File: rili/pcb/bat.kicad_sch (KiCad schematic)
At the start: 21 parts, among them J1 Battery, Q3 AO3407, Q4 FS8205, SW1 SW_SPDT, U3 TP4056-42-ESOP8, U4 MCP1700x-330xxTT, U5 DW01A

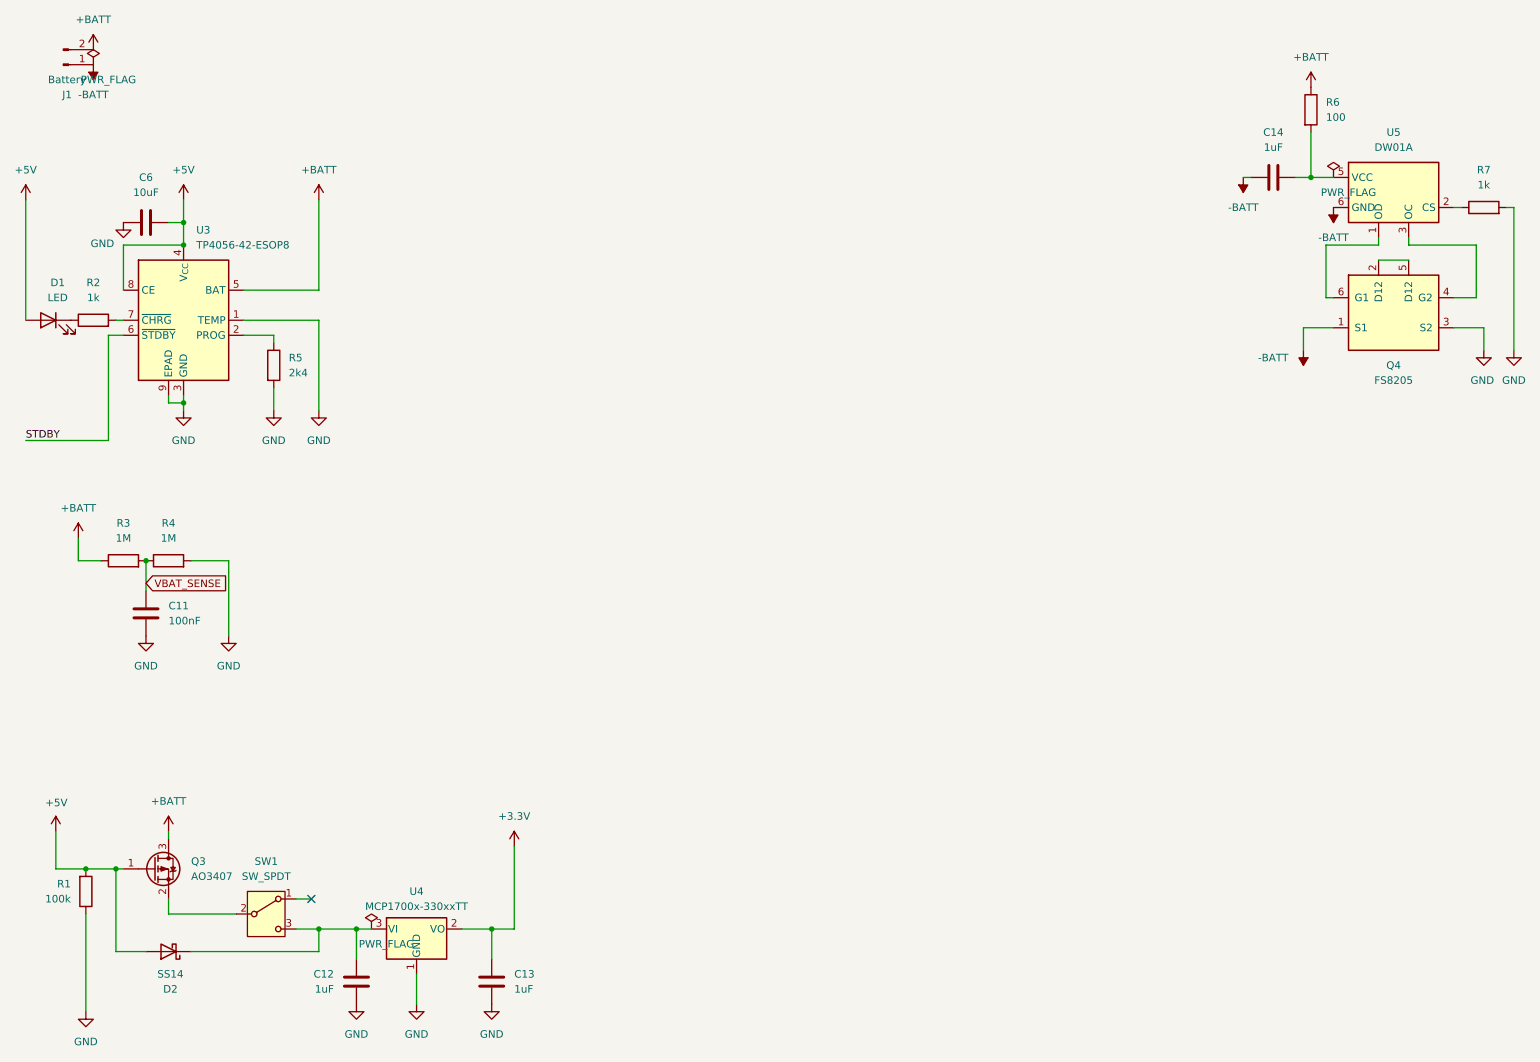
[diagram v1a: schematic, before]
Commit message: layout v2 : carte routée — PCB↔schéma réconciliés, BOM LCSC, TVS matrice, DRC 990→24
- réconciliation PCB↔schéma en une passe : 105 empreintes remariées (matrice ×2,
  module P4), 54 périmées supprimées, ~140 importées par F8 ; footprint TRRS
  MJ-4PP-9_rev3 créé (pads mappés de l'ancien design fonctionnel)
- placement : moitié droite générée au miroir exact du pré-placement gauche
  (axe x=188.46048), trous de montage symétrisés, origine de grille sur l'axe
- protection ESD matrice : 22 SD05C-01F (un par ligne, côté switchs des 100R,
  validés par partition de netlist) ; PWR_FLAG +5V_D réparé
- BOM LCSC dans les propriétés des symboles (32 composants : réfs, liens,
  notes d'achat) + annexe courses complète au plan v2 ; connecteur trackpad
  corrigé (ZIF Hirose FH12-6S-0.5SH, réf MNT Reform)
- règles JLCPCB (planchers DRC + classes Default/Power re-branchées v2),
  passage 4 couches, routage complet des deux moitiés
- gerbers v1 corne-cherry retirés (obsolètes)
- baselines tripwire re-référencées : DRC 990→24 erreurs / 208→17 warnings,
  ERC 0 erreur / 200 warnings (53 fantômes headless documentés)

Co-Authored-By: Claude Fable 5 <noreply@anthropic.com>
Claude-Session: https://claude.ai/code/session_01GfX5RmekmQi78Dm37qsT4Z
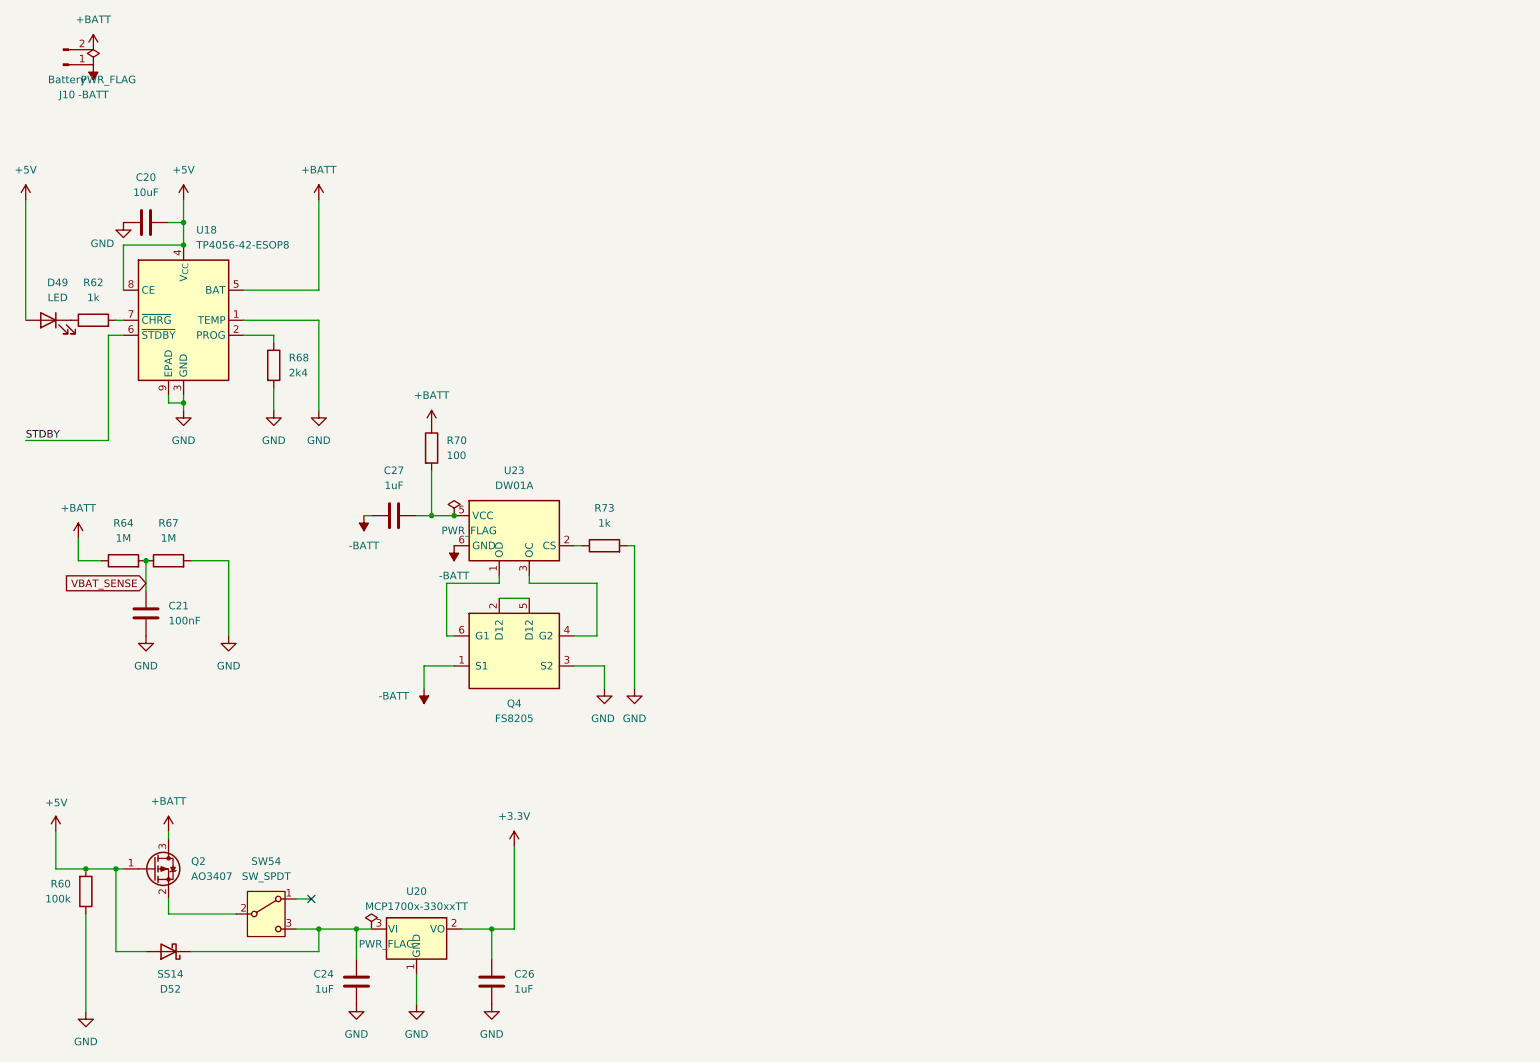
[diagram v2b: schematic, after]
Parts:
- C20: renamed from C6; footprint Capacitor_SMD:C_1210_3225Metric_Pad1.33x2.70mm_HandSolder -> Capacitor_SMD:C_1206_3216Metric_Pad1.33x1.80mm_HandSolder
- D52: renamed from D2; LCSC (none) -> C2480; Lien (none) -> https://lcsc.com/product-detail/C2480.html
- Q2: renamed from Q3; LCSC (none) -> C351408; Lien (none) -> https://lcsc.com/product-detail/C351408.html
- Q4: LCSC (none) -> C32254; Lien (none) -> https://lcsc.com/product-detail/C32254.html
- SW54: renamed from SW1; LCSC (none) -> C431540; Lien (none) -> https://lcsc.com/product-detail/C431540.html; Note achat (none) -> MSK-12C02 SHOU HAN
- U18: renamed from U3; LCSC (none) -> C16581; Lien (none) -> https://lcsc.com/product-detail/C16581.html
- U20: renamed from U4; LCSC (none) -> C39051; Lien (none) -> https://lcsc.com/product-detail/C39051.html
- U23: renamed from U5; LCSC (none) -> C351410; Lien (none) -> https://lcsc.com/product-detail/C351410.html
- renumbered C11 to C21, C12 to C24, C13 to C26, C14 to C27, D1 to D49, J1 to J10, R1 to R60, R2 to R62, R3 to R64, R4 to R67, R5 to R68, R6 to R70, R7 to R73
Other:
- moved on the sheet: C27, Q4, R70, R73, U23

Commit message: layout : panneau vertical 2 rails dans le dépôt + baseline chantier
Panneau 185×212 (droite tournée 180°, rails + 8 tabs mouse-bites) appliqué par
Mae, F8 des passifs unifiés. Baseline DRC re-référencée 24/19 → 36/26 (état
panneau, finitions DRC prévues : pistes près des lignes de rupture, vias de
maillage orphelins dans les bandes sans cuivre).

Co-Authored-By: Claude Fable 5 <noreply@anthropic.com>
Claude-Session: https://claude.ai/code/session_01GfX5RmekmQi78Dm37qsT4Z
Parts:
- C21: footprint Capacitor_SMD:C_0805_2012Metric_Pad1.18x1.45mm_HandSolder -> Capacitor_SMD:C_0603_1608Metric
- R60, R70: footprint Resistor_SMD:R_0805_2012Metric_Pad1.20x1.40mm_HandSolder -> Resistor_SMD:R_0603_1608Metric
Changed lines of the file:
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@@
 			)
 		)
-		(property "Footprint" "Resistor_SMD:R_0805_2012Metric_Pad1.20x1.40mm_HandSolder"
+		(property "Footprint" "Resistor_SMD:R_0603_1608Metric"
 			(at 28.702 163.83 90)
 			(hide yes)
@@
 			)
 		)
-		(property "Footprint" "Resistor_SMD:R_0805_2012Metric_Pad1.20x1.40mm_HandSolder"
+		(property "Footprint" "Resistor_SMD:R_0603_1608Metric"
 			(at 87.122 88.9 90)
 			(hide yes)
@@
 			)
 		)
-		(property "Footprint" "Capacitor_SMD:C_0805_2012Metric_Pad1.18x1.45mm_HandSolder"
+		(property "Footprint" "Capacitor_SMD:C_0603_1608Metric"
 			(at 39.6748 113.03 0)
 			(hide yes)

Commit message: review schéma : LDO S3 corrigé (pins SOT-89) + 8 valeurs — HT7833 en place
Revue 4 relecteurs parallèles avant commande, validée ligne à ligne sur la
netlist. BLOQUANT réparé : U20/U21 avaient le brochage SOT-23 du MCP1700 sur
des pastilles SOT-89 → entrée/sortie inversées pour tout LDO réel ; pins 2/3
échangés dans la déf, Value=HT7833 (C50936), F8 + reroutage des 2 zones par
Mae, pads vérifiés (1=GND 2=VIN 3=VOUT). Valeurs : bulk 3V3 C11/C12 et condos
LDO C23-C26 → 10µF (C15850), CHIP_PU P4 R54→10k C14→1µF. Baseline ERC 200→202
(lib_symbol_mismatch des défs LDO éditées). Validé par la revue : chaînes
batterie/charge/load-share, paires USB bout en bout, hub, prog P4 ×2 ports,
microSD IOMUX+pullups, strapping, nRF24, trackpad, 22 TVS matrice.

Co-Authored-By: Claude Fable 5 <noreply@anthropic.com>
Claude-Session: https://claude.ai/code/session_01GfX5RmekmQi78Dm37qsT4Z
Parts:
- C21: footprint Capacitor_SMD:C_0603_1608Metric -> Capacitor_SMD:C_0603_1608Metric_Pad1.08x0.95mm_HandSolder
- C24, C26: value 1uF -> 10uF; footprint Capacitor_SMD:C_0805_2012Metric_Pad1.18x1.45mm_HandSolder -> Capacitor_SMD:C_1206_3216Metric_Pad1.33x1.80mm_HandSolder
- R60, R70: footprint Resistor_SMD:R_0603_1608Metric -> Resistor_SMD:R_0603_1608Metric_Pad0.98x0.95mm_HandSolder
- U20: value MCP1700x-330xxTT -> HT7833; LCSC C39051 -> C50936; Lien https://lcsc.com/product-detail/C39051.html -> https://lcsc.com/product-detail/C50936.html
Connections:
- net +3.3V: now also U20.3 (VO); no longer U20.2 (VO)
- net at C24.2, D52.1 (K), SW54.3 (C): now also U20.2 (VI); no longer U20.3 (VI)
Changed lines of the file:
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@@
 			)
 		)
-		(property "Footprint" "Resistor_SMD:R_0603_1608Metric"
+		(property "Footprint" "Resistor_SMD:R_0603_1608Metric_Pad0.98x0.95mm_HandSolder"
 			(at 28.702 163.83 90)
 			(hide yes)
@@
 			)
 		)
-		(property "Footprint" "Resistor_SMD:R_0603_1608Metric"
+		(property "Footprint" "Resistor_SMD:R_0603_1608Metric_Pad0.98x0.95mm_HandSolder"
 			(at 87.122 88.9 90)
 			(hide yes)
@@
 			)
 		)
-		(property "Value" "1uF"
+		(property "Value" "10uF"
 			(at 102.87 180.3399 0)
 			(show_name no)
@@
 			)
 		)
-		(property "Footprint" "Capacitor_SMD:C_0805_2012Metric_Pad1.18x1.45mm_HandSolder"
+		(property "Footprint" "Capacitor_SMD:C_1206_3216Metric_Pad1.33x1.80mm_HandSolder"
 			(at 98.0948 175.26 0)
 			(hide yes)
@@
 			)
 		)
-		(property "Value" "1uF"
+		(property "Value" "10uF"
 			(at 72.39 180.3399 0)
 			(show_name no)
@@
 			)
 		)
-		(property "Footprint" "Capacitor_SMD:C_0805_2012Metric_Pad1.18x1.45mm_HandSolder"
+		(property "Footprint" "Capacitor_SMD:C_1206_3216Metric_Pad1.33x1.80mm_HandSolder"
 			(at 77.1652 175.26 0)
 			(hide yes)
@@
 			)
 		)
-		(property "Value" "MCP1700x-330xxTT"
+		(property "Value" "HT7833"
 			(at 86.36 166.37 0)
 			(show_name no)
@@
 			)
 		)
-		(property "LCSC" "C39051"
+		(property "LCSC" "C50936"
 			(at 86.36 170.18 0)
 			(hide yes)
@@
 			)
 		)
-		(property "Lien" "https://lcsc.com/product-detail/C39051.html"
+		(property "Lien" "https://lcsc.com/product-detail/C50936.html"
 			(at 86.36 170.18 0)
 			(hide yes)
@@
 			)
 		)
-		(property "Footprint" "Capacitor_SMD:C_0603_1608Metric"
+		(property "Footprint" "Capacitor_SMD:C_0603_1608Metric_Pad1.08x0.95mm_HandSolder"
 			(at 39.6748 113.03 0)
 			(hide yes)
